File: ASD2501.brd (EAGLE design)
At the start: 22.5 x 30.5 mm, 24 parts, among them J1 DF12-32-DP, J2 DF12-32-DS, U1 XC6210B18, U2 JF2, U3 TXS0102, U4 TXS0102, Y1 ANT

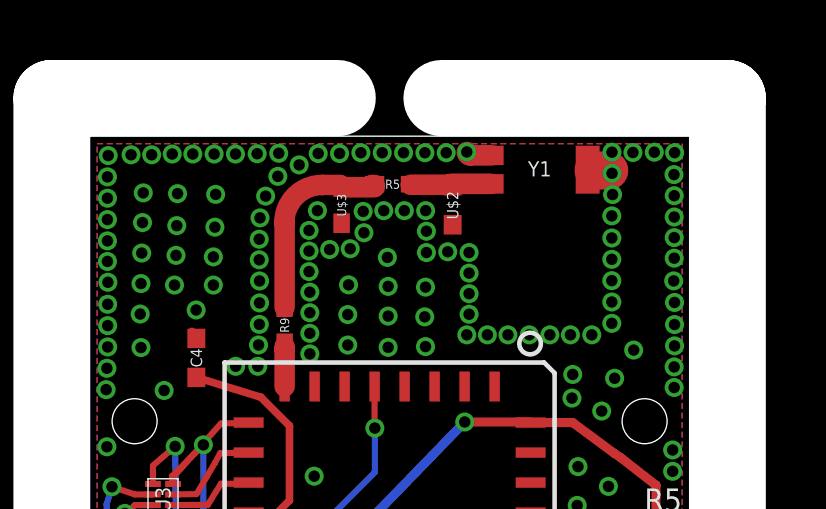
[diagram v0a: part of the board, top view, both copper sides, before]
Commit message: Updated antenna ref des
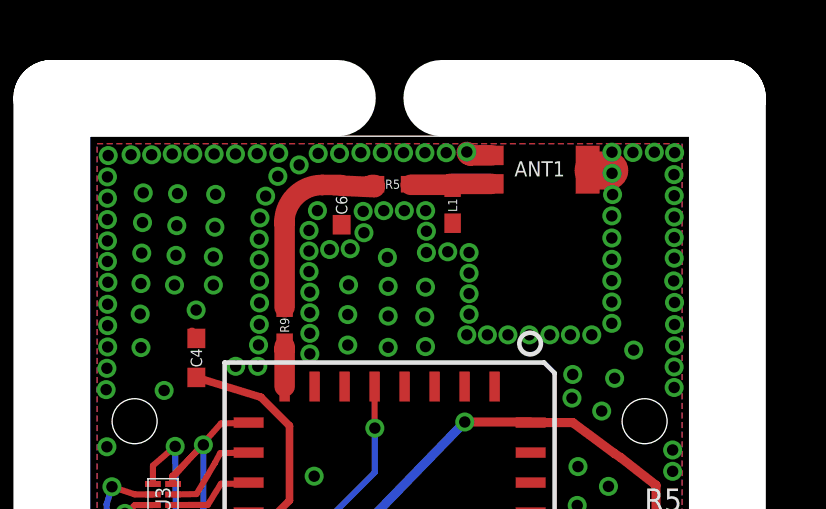
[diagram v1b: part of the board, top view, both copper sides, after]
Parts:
- removed U$2: 0.5pF, tinycircuits:C0402
- removed U$3: 1nH, tinycircuits:0402
- removed Y1: ANT, akrosense:W3011
- added ANT1: AS-ITM-00109, tinycircuits:W3011
- added C6: 0.5pF, tinycircuits:C0402
- added L1: 1nH, tinycircuits:0402
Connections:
- net GND: now also ANT1.2, ANT1.3, C6.2, L1.2; no longer U$2.2, U$3.2, Y1.2, Y1.3
- net N$1: now also C6.1; no longer U$3.1
- net N$5: now also ANT1.1, L1.1; no longer U$2.1, Y1.1
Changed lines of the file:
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@@
 <attribute name="DATABASE" value="./../../../../../Components/TinyCircuits_Part_Database.txt" x="27.8638" y="16.454" size="1.778" layer="27" rot="R270" display="off"/>
 </element>
-<element name="Y1" library="akrosense" package="W3011" value="ANT" x="25" y="36.8864" rot="R180"/>
+<element name="ANT1" library="tinycircuits" package="W3011" value="AS-ITM-00109" x="25" y="36.8864" rot="R180">
+<attribute name="PARTNO" value="AS-ITM-00109" x="25" y="36.8864" size="1.778" layer="27" rot="R180" display="off"/>
+<attribute name="VALUE" value="W3011A" x="25" y="36.8864" size="1.778" layer="27" rot="R180" display="off"/>
+</element>
 <element name="R2" library="tinycircuits" package="0402_SHORT" value="0.0" x="14.7066" y="19.05" rot="MR180"/>
 <element name="R3" library="tinycircuits" package="0402_SHORT" value="0.0" x="14.6812" y="20.1676" rot="MR180"/>
@@
 <attribute name="VALUE" value="0.0" x="16.5" y="31.7" size="1.778" layer="27" rot="R270" display="off"/>
 </element>
-<element name="U$2" library="tinycircuits" package="C0402" value="0.5pF" x="22.1" y="35.7" rot="R270">
-<attribute name="VALUE" value="0.5pF" x="22.1" y="35.7" size="1.778" layer="27" rot="R270" display="off"/>
-</element>
-<element name="U$3" library="tinycircuits" package="0402" value="1nH" x="18.4" y="35.7" rot="R270">
-<attribute name="VALUE" value="1nH" x="18.4" y="35.7" size="1.778" layer="27" rot="R270" display="off"/>
+<element name="L1" library="tinycircuits" package="0402" value="1nH" x="22.1" y="35.7" rot="R270">
+<attribute name="VALUE" value="1nH" x="22.1" y="35.7" size="1.778" layer="27" rot="R270" display="off"/>
+</element>
+<element name="C6" library="tinycircuits" package="C0402" value="0.5pF" x="18.4" y="35.7" rot="R270">
+<attribute name="VALUE" value="0.5pF" x="18.4" y="35.7" size="1.778" layer="27" rot="R270" display="off"/>
 </element>
 </elements>
@@
 <contactref element="C1" pad="2"/>
 <contactref element="U3" pad="4"/>
-<contactref element="Y1" pad="3"/>
-<contactref element="Y1" pad="2"/>
+<contactref element="ANT1" pad="3"/>
+<contactref element="ANT1" pad="2"/>
 <polygon width="0.254" layer="1">
 <vertex x="10.25" y="37.75"/>
@@
 <wire x1="26.797" y1="36.8554" x2="27.32228125" y2="36.8554" width="1.27" layer="1"/>
 <wire x1="27.32228125" y1="36.8554" x2="27.414221875" y2="36.763459375" width="0.6858" layer="1" curve="-90"/>
-<contactref element="U$2" pad="2"/>
-<contactref element="U$3" pad="2"/>
+<contactref element="L1" pad="2"/>
+<contactref element="C6" pad="2"/>
 <wire x1="28.82391875" y1="37.467034375" x2="28.11018125" y2="37.456875" width="0" layer="19" extent="1-1"/>
 <wire x1="29.4995625" y1="37.451796875" x2="28.82391875" y2="37.467034375" width="0" layer="19" extent="1-1"/>
@@
 <wire x1="17.340578125" y1="30.74365625" x2="17.340578125" y2="31.42945625" width="0" layer="19" extent="1-1"/>
 <wire x1="17.594578125" y1="35.51885625" x2="17.315178125" y2="34.85845625" width="0" layer="19" extent="1-1"/>
-<wire x1="22.1" y1="35.05" x2="21.937978125" y2="34.14725625" width="0" layer="19" extent="1-1"/>
+<wire x1="22.1" y1="35.1" x2="21.937978125" y2="34.14725625" width="0" layer="19" extent="1-1"/>
 <wire x1="17.5" y1="29.655" x2="17.340578125" y2="30.74365625" width="0" layer="19" extent="1-1"/>
 <wire x1="28.135578125" y1="30.87065625" x2="27.406603125" y2="31.762196875" width="0" layer="19" extent="1-1"/>
@@
 <wire x1="13.2842" y1="10.7442" x2="10.8712" y2="13.1318" width="0" layer="19" extent="1-1"/>
 <wire x1="21.25" y1="12.4999" x2="27.404065625" y2="13.2735375" width="0" layer="19" extent="16-16"/>
-<wire x1="18.4" y1="35.1" x2="13.2842" y2="10.7442" width="0" layer="19" extent="1-1"/>
+<wire x1="18.4" y1="35.05" x2="13.2842" y2="10.7442" width="0" layer="19" extent="1-1"/>
 </signal>
 <signal name="AREF">
@@
 </signal>
 <signal name="N$5">
-<contactref element="Y1" pad="1"/>
+<contactref element="ANT1" pad="1"/>
 <wire x1="23.4" y1="36.4114" x2="22.027840625" y2="36.4114" width="0.6858" layer="1"/>
 <contactref element="R5" pad="1"/>
 <wire x1="20.7" y1="36.379740625" x2="20.7" y2="36.4" width="0.4064" layer="1"/>
-<contactref element="U$2" pad="1"/>
+<contactref element="L1" pad="1"/>
 <wire x1="20.7" y1="36.379740625" x2="22.1" y2="36.379740625" width="0.6858" layer="1"/>
-<wire x1="22.1" y1="36.379740625" x2="22.1" y2="36.35" width="0.4064" layer="1"/>
+<wire x1="22.1" y1="36.379740625" x2="22.1" y2="36.3" width="0.4064" layer="1"/>
 <wire x1="22.1" y1="36.379740625" x2="22.027840625" y2="36.4114" width="0" layer="19" extent="1-1"/>
 </signal>
@@
 <wire x1="16.48968125" y1="35.115503125" x2="16.5" y2="35.115503125" width="0.4064" layer="1"/>
 <wire x1="16.5" y1="35.115503125" x2="16.5" y2="32.3" width="0.6858" layer="1"/>
-<contactref element="U$3" pad="1"/>
+<contactref element="C6" pad="1"/>
 <wire x1="18.35424375" y1="36.37534375" x2="18.4" y2="36.37534375" width="0.4064" layer="1"/>
-<wire x1="18.4" y1="36.37534375" x2="18.4" y2="36.3" width="0.4064" layer="1"/>
-<wire x1="18.4" y1="36.3" x2="19.5" y2="36.3" width="0.6858" layer="1"/>
+<wire x1="18.4" y1="36.37534375" x2="18.4" y2="36.35" width="0.4064" layer="1"/>
+<wire x1="18.4" y1="36.35" x2="19.5" y2="36.3" width="0.6858" layer="1"/>
 <wire x1="19.5" y1="36.3" x2="19.5" y2="36.4" width="0.4064" layer="1"/>
 </signal>
